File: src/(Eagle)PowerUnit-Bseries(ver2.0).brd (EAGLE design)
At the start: 105 x 137 mm, 315 parts, among them CON1 XT60PW-F, CON2 XT60PW-F, CON3 XT60PW-F, CON4 XT60PW-F, CON5 XT90PW-F, Q1 SQJA16EP-T1_GE3, Q10 SQJA16EP-T1_GE3, Q11 TMBT3906, Q12 TMBT3906, Q2 SSM3J332R, Q6 SQJA16EP-T1_GE3, SW1 SS-12SDP2, SW2 RDS-16S-1055-SMT-TR, SW3 SSSS213202, SW4 2MS1-T2-B4-M2-Q-E-S, SW5 2MS1-T2-B4-M2-Q-E-S, U1 LQFP64, U10 TC7S14F, U11 MCP6541T-I/LT, U12 MCP6541T-I/LT, U13 TC7S14F, U14 TCK420G, U15 TCKE805NAWSON10B_TOS-REC, U16 TC7SH00FULJ, U17 TC7S14F, U18 TC7S14F, U19 TC7SH00FULJ, U2 MCP2517FD, U20 TLP293, U21 TC7S14F, U22 TC7S14F, U23 TC7S14F, U24 MCP6541T-I/LT, U25 TC7S14F, U26 TC7SH00FULJ, U27 MCP6541T-I/LT, U3 CH340E, U4 CZ-3A04, U5 AP63205WU-7, U6 CZ-3A04, U7 MCP6541T-I/LT, U8 CZ-3A04, U9 CZ-3A04, X1 XRCGB40M000F4M01R0, X2 RH100-24.000-18-1020-EXT-TR, X3 32.768K12.5PI/MC306

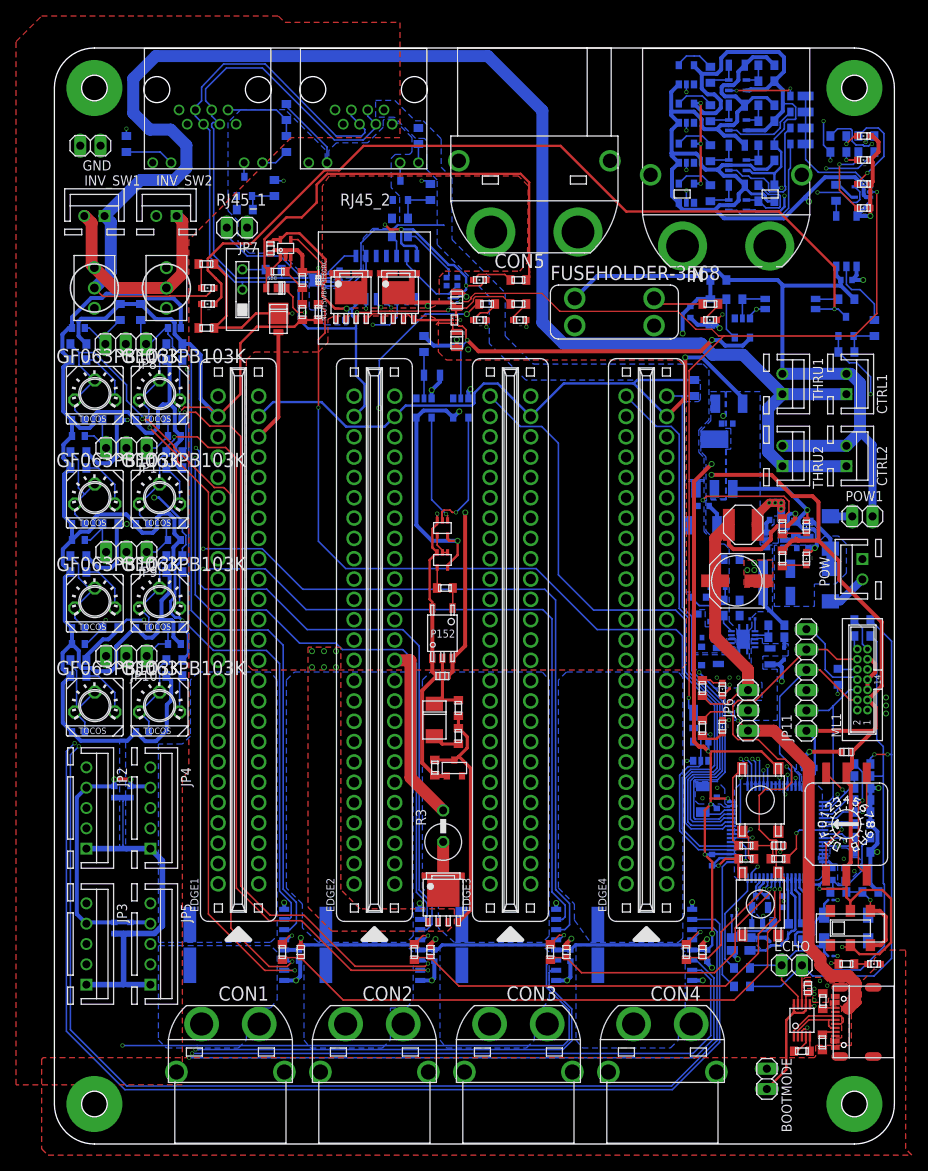
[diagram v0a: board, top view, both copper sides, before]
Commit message: DRC OK,before I move it KiCad.
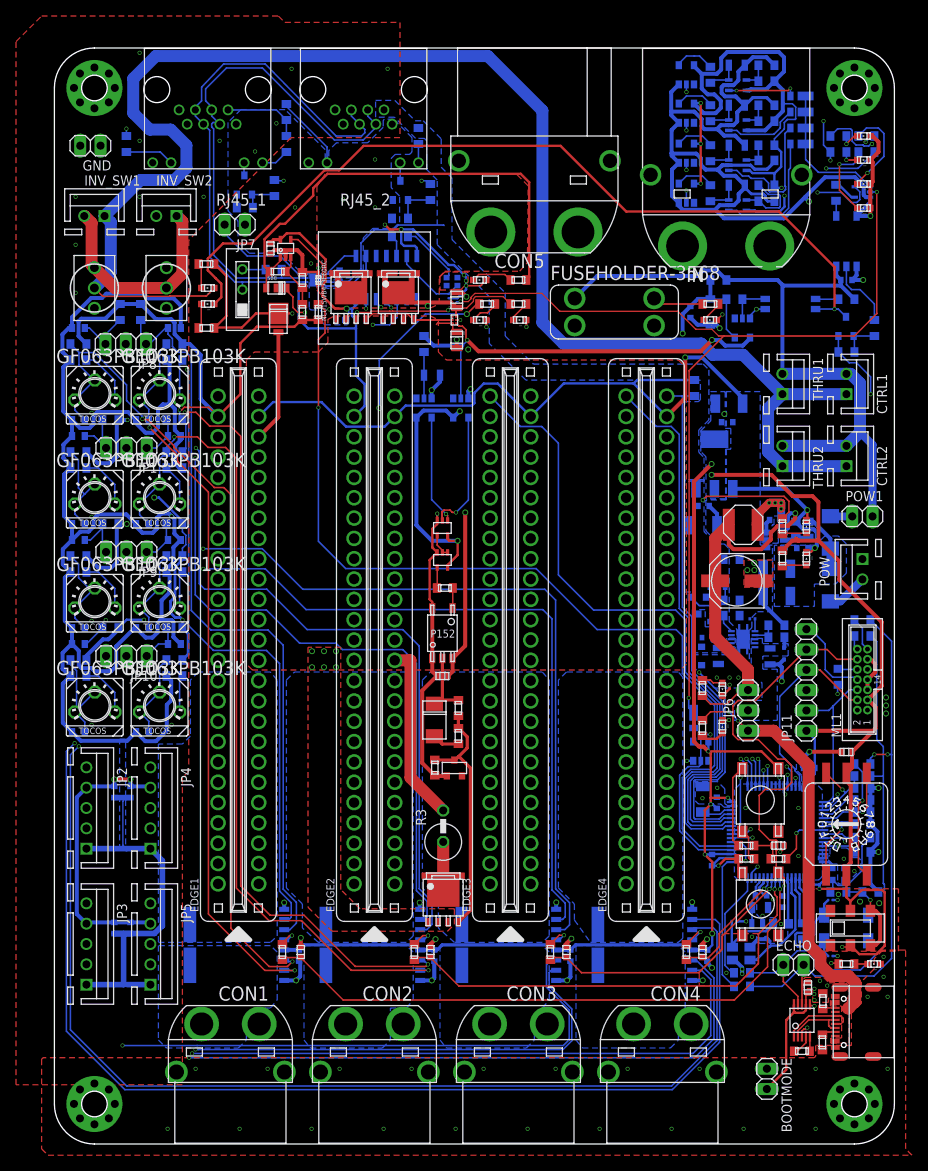
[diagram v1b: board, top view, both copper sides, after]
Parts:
- moved X2 1.20 mm to (85.8, 18.8)
- moved C28 0.73 mm to (85.0, 22.8)
- moved R16 0.60 mm to (86.0, 16.4)
- moved JP7 0.46 mm to (22.6, 109.9)
- moved R37 0.24 mm to (23.8, 112.0)
- moved ECHO 0.22 mm to (92.4, 17.4)
- moved TR1 0.18 mm to (22.8, 113.7)
- moved C11 0.17 mm to (84.1, 85.2)
- moved C22 0.09 mm to (88.3, 26.1)
- moved C3 0.08 mm to (94.2, 14.6)
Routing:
- net ENC1_A: track 162.7 -> 160.0 mm
- net ENC2_B: track 151.0 -> 148.6 mm
- net ENC1_B: track 162.9 -> 160.5 mm
- net SGND: track 648.4 -> 650.7 mm, vias 53 -> 130
- net ENC3_B: track 145.6 -> 143.3 mm
- net ENC4_A: track 138.2 -> 136.0 mm
- net ENC2_A: track 141.1 -> 139.1 mm
- net NRST: track 56.5 -> 54.5 mm
- net ENC4_B: track 147.4 -> 145.6 mm
- net ENC3_A: track 149.4 -> 147.8 mm
- net N$54: track 8.58 -> 10.1 mm
- net N$63: track 12.1 -> 10.8 mm
- net CURRENT3: track 36.2 -> 35.1 mm
- net N$87: track 112.7 -> 111.6 mm
- net CURRENT2: track 56.6 -> 57.6 mm
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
